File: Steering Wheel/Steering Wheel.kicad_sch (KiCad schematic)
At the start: 29 parts, among them J1 DTF13-4P, J2 Upshift Paddle, J3 Downshift Paddle, J4 Neutral Button, J5 Start Button, J6 Unused Button 1, J7 Unused Button 2, J8 Selection Knob, U1 AS1115-BSST, U2 CC56-12GWA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

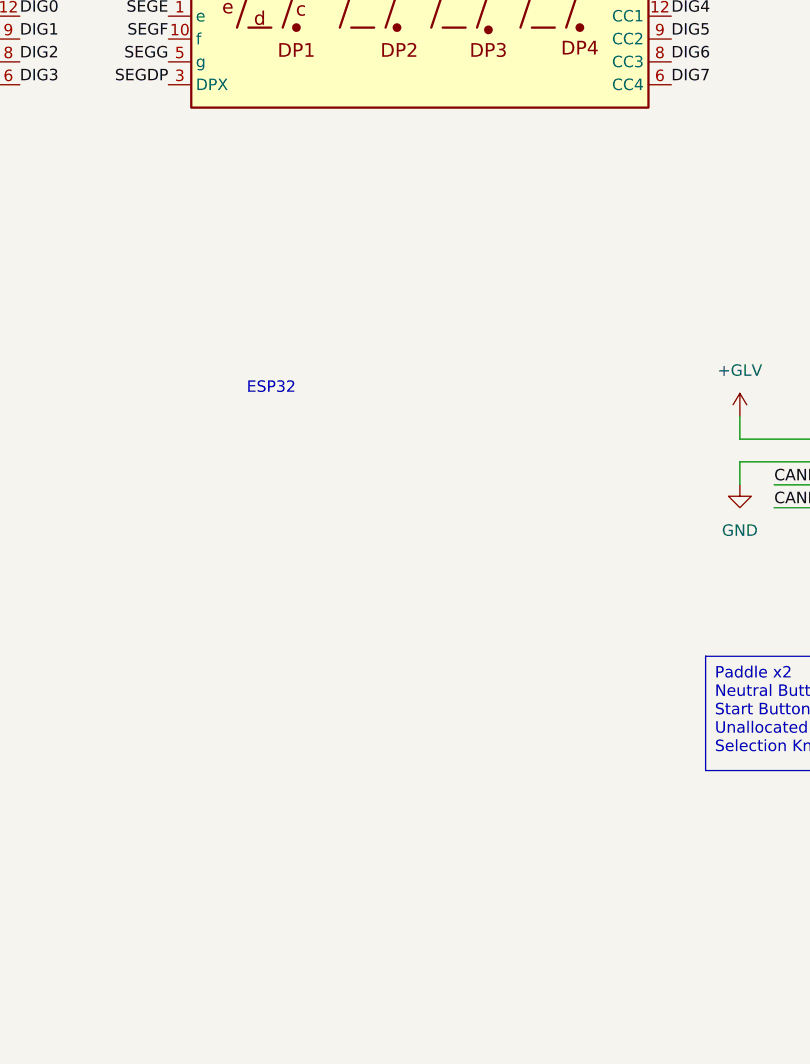
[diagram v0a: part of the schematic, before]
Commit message: feat: begin SCU, RLM, PCU, ETC. update SWU
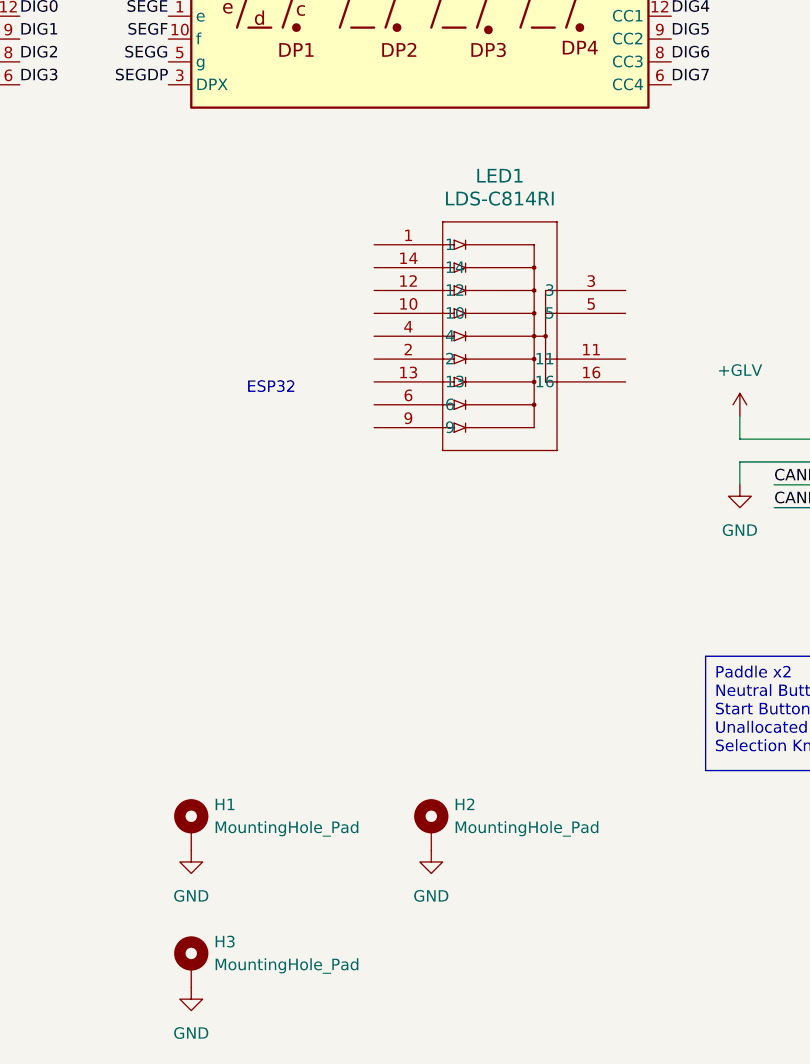
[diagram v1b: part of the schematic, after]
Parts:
- added H1, H2, H3: MountingHole_Pad, MountingHole:MountingHole_6.5mm_Pad, symbol Mechanical:MountingHole_Pad
- added LED1: LDS-C814RI, LDS-C814RI_LUM, symbol LDS-C814RI_LUM:LDS-C814RI
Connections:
- net GND: now also H1.1, H2.1, H3.1
